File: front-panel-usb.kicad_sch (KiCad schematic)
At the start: 75 parts, among them J3 USB-C_GCT_USB4105-GF-A, J4 USB-C_GCT_USB4105-GF-A, J5 USB-C_GCT_USB4105-GF-A, Q29 BSS84AKW, U11 TPD4E05U06QDQARQ1, U13 FT4232H_VQFN, U15 NCP718BSN330T1G, U3 AP22615A_TSOT26, U5 AP22615A_TSOT26, U6 TPD4E05U06QDQARQ1, U7 TPD4E05U06QDQARQ1, Y1 Resonator_12MHz_ABM8G

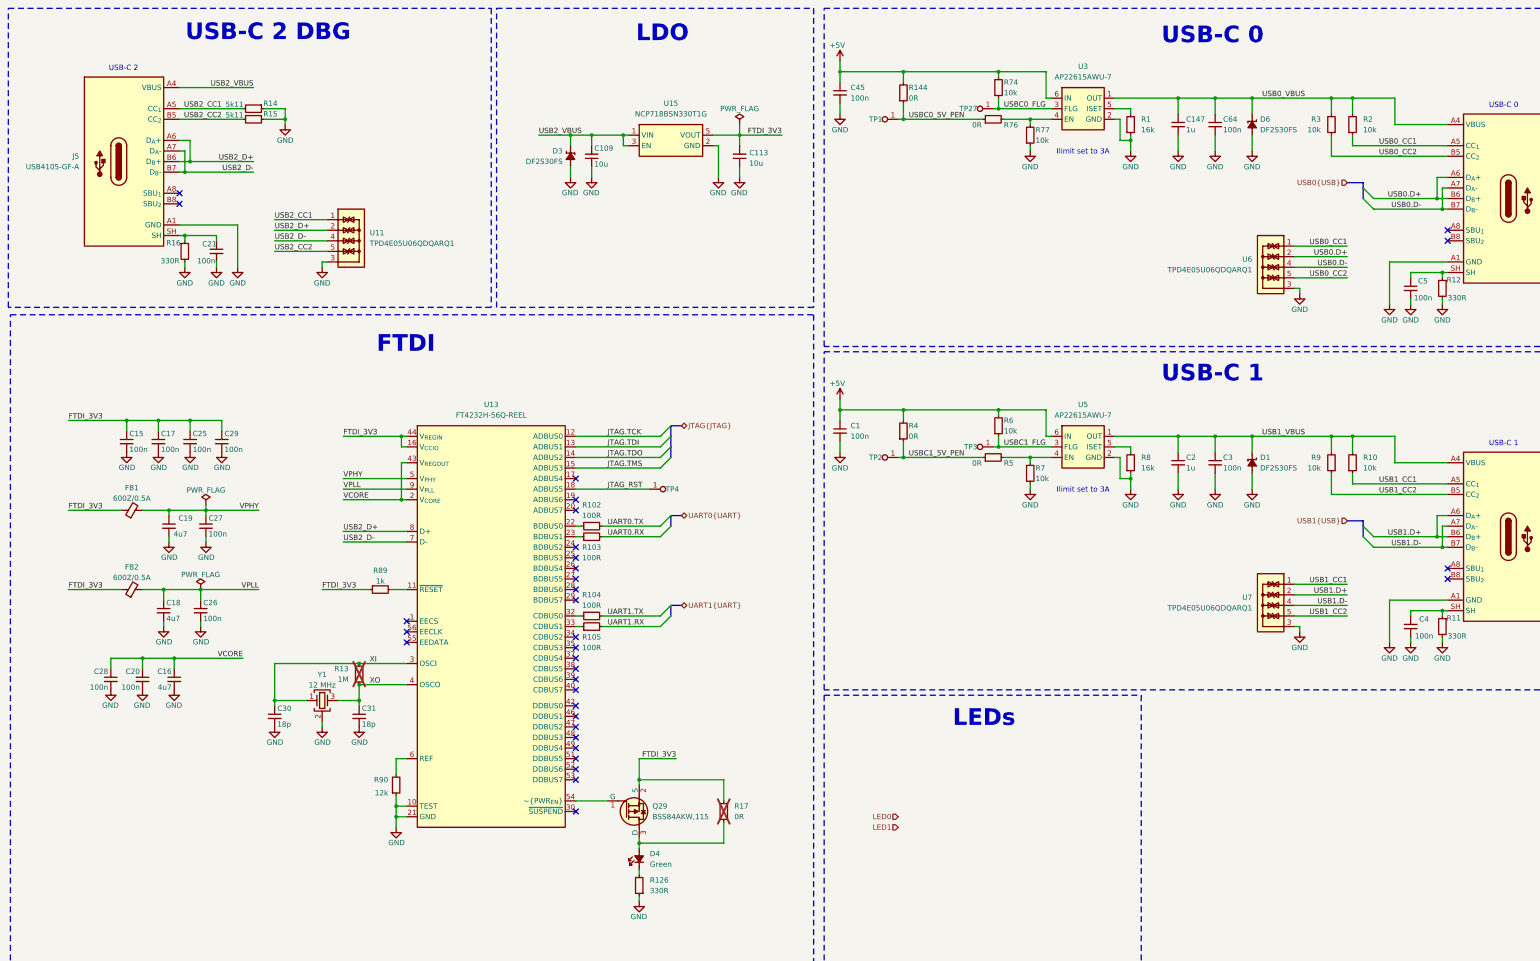
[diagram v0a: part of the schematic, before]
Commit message: [#82176] Fix conflicting annotations
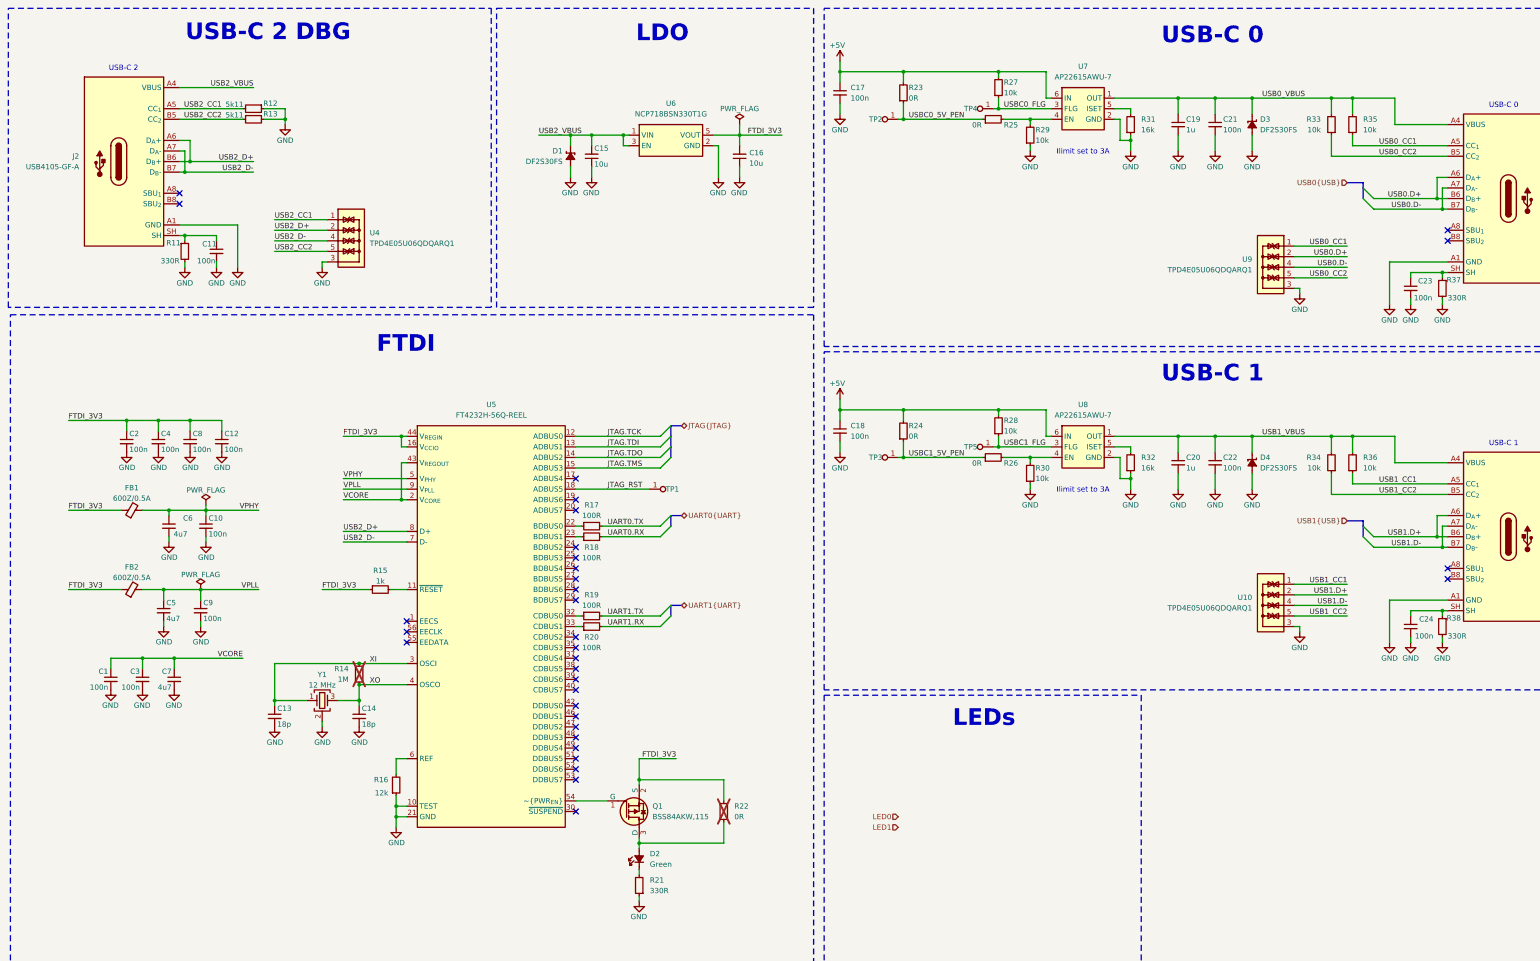
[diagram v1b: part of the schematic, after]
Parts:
- renumbered C28 to C1, C27 to C10, C21 to C11, C29 to C12, C30 to C13, C31 to C14, C109 to C15, C113 to C16, C45 to C17, C1 to C18, C147 to C19, C15 to C2, C2 to C20, C64 to C21, C3 to C22, C5 to C23, C4 to C24, C20 to C3, C17 to C4, C18 to C5, C19 to C6, C16 to C7, C25 to C8, C26 to C9, D3 to D1, D4 to D2, D6 to D3, D1 to D4, J5 to J2, Q29 to Q1, R16 to R11, R14 to R12, R15 to R13, R13 to R14, R89 to R15, R90 to R16, R102 to R17, R103 to R18, R104 to R19, R105 to R20, R126 to R21, R17 to R22, R144 to R23, R4 to R24, R76 to R25, R5 to R26, R74 to R27, R6 to R28, R77 to R29, R7 to R30, R1 to R31, R8 to R32, R3 to R33, R9 to R34, R2 to R35, R10 to R36, R12 to R37, R11 to R38, TP4 to TP1, TP1 to TP2, TP2 to TP3, TP27 to TP4, TP3 to TP5, U7 to U10, U11 to U4, U13 to U5, U15 to U6, U3 to U7, U5 to U8, U6 to U9

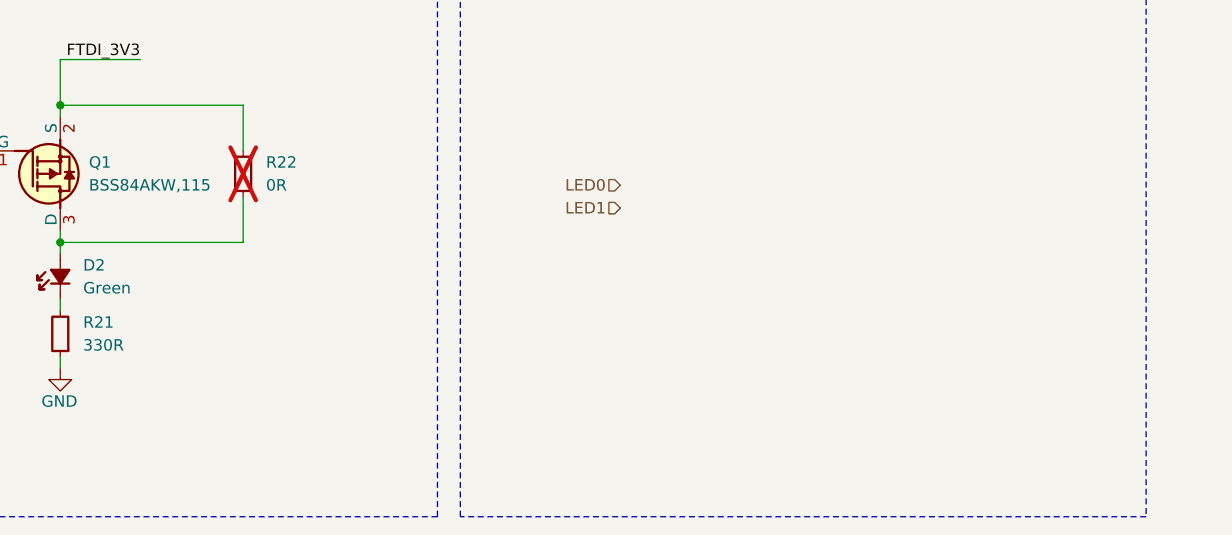
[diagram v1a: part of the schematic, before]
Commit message: Add light pipe and one additional LED
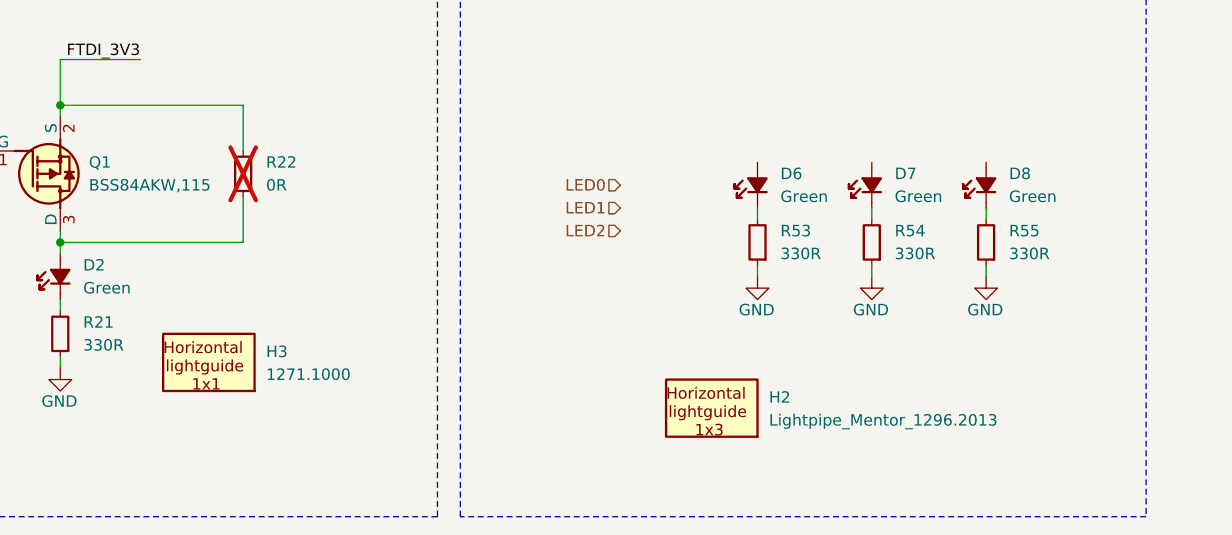
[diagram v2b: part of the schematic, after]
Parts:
- added D6, D7, D8: LED_G_0402_VLMTG1500-GS08, antmicro-footprints:LED_0402_1005Metric_G, symbol antmicroLEDIndicationDiscrete:LED_G_0402_VLMTG1500-GS08
- added H2: Lightpipe_Mentor_1296.2013, antmicro-footprints:Mech_Lightpipe_Mentor_1296.2013, symbol antmicroMechanicalParts:Lightpipe_Mentor_1296.2013
- added H3: Lightpipe_Mentor_1271.1000, antmicro-footprints:Mech_Lightpipe_Mentor_1271.1000, symbol antmicroMechanicalParts:Lightpipe_Mentor_1271.1000
- added R53, R54, R55: R_330R_0402, antmicro-footprints:R_0402_1005Metric, symbol antmicroResistors0402:R_330R_0402
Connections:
- net GND: now also R53.1, R54.1, R55.1
- new net: D7.1 (C), R54.2
- new net: D8.1 (C), R55.2
- new net: D6.1 (C), R53.2

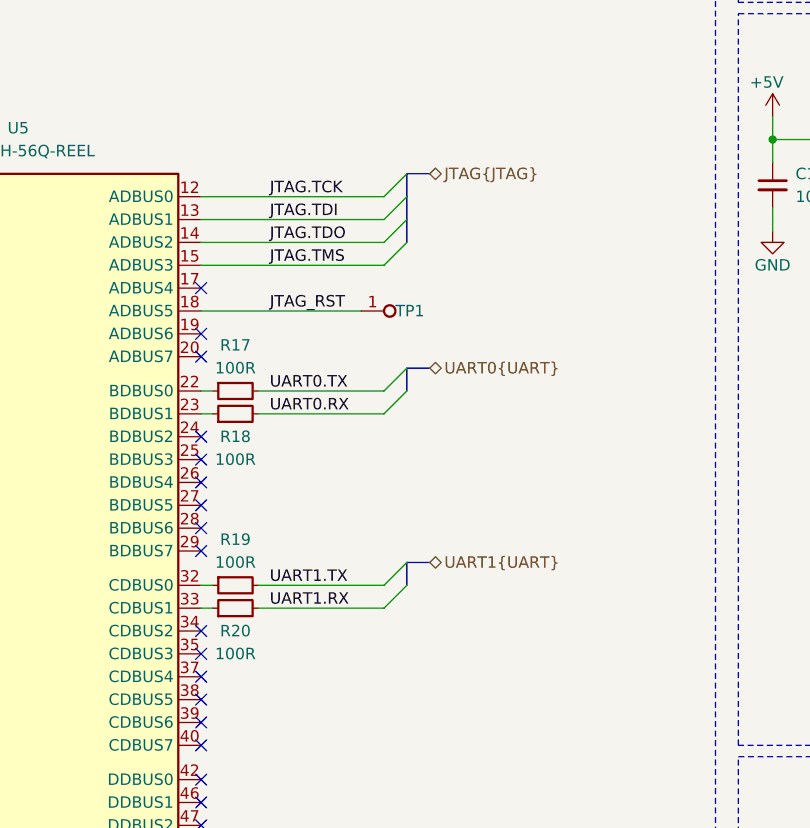
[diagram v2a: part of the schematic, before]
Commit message: Add series resistors to JTAG lines
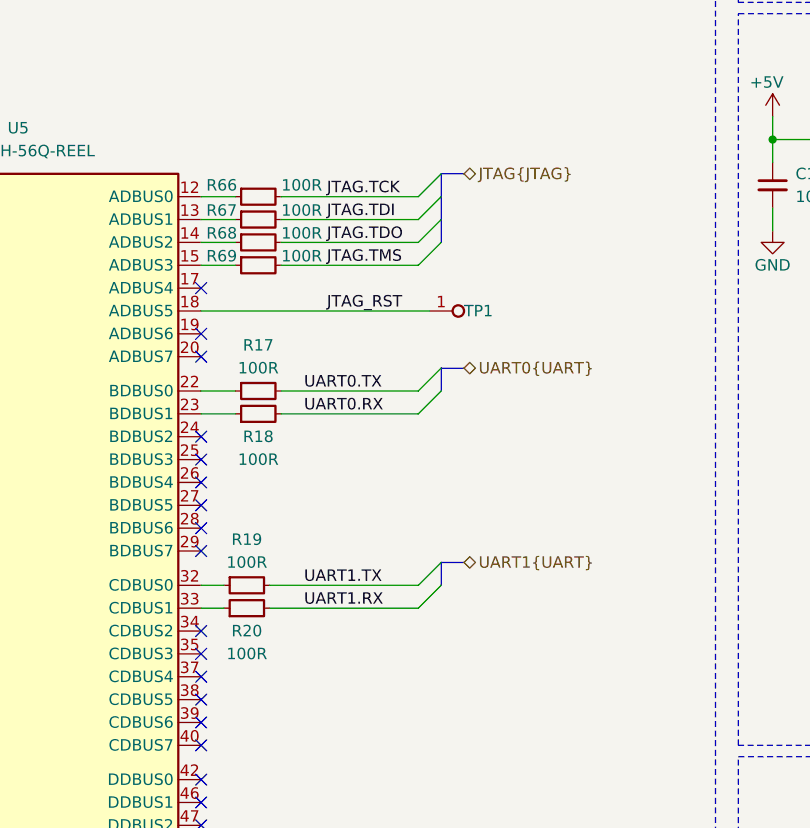
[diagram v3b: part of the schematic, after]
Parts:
- added R66, R67, R68, R69: R_100R_0402, antmicro-footprints:R_0402_1005Metric, symbol antmicroResistors0402:R_100R_0402
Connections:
- net JTAG.TCK: now also R66.2; no longer U5.12 (ADBUS0)
- net JTAG.TDI: now also R67.2; no longer U5.13 (ADBUS1)
- net JTAG.TDO: now also R68.2; no longer U5.14 (ADBUS2)
- net JTAG.TMS: now also R69.2; no longer U5.15 (ADBUS3)
- new net: R66.1, U5.12 (ADBUS0)
- new net: R67.1, U5.13 (ADBUS1)
- new net: R68.1, U5.14 (ADBUS2)
- new net: R69.1, U5.15 (ADBUS3)
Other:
- moved on the sheet: R17, R18, R19, R20, TP1

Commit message: Replace USB-C connectors with vertical version
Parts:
- removed J2, J3, J4: USB-C_GCT_USB4105-GF-A, antmicro-footprints:USB-C_Receptacle_GCT_USB4105-GF-A, symbol antmicroUSBConnectors:USB-C_GCT_USB4105-GF-A
- removed R66, R67, R68, R69: R_100R_0402, antmicro-footprints:R_0402_1005Metric, symbol antmicroResistors0402:R_100R_0402
- added J2, J3, J4: USB-C_Kycon_KUSBX-SL2-CS1N24-B-TR, antmicro-footprints:USB-C_Receptacle_Kycon_KUSBX-SL2-CS1N24-B-TR, symbol antmicroUSBConnectors:USB-C_Kycon_KUSBX-SL2-CS1N24-B-TR
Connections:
- net GND: now also J2.A1 (GND), J2.A12 (GND), J2.B1 (GND), J2.B12 (GND), J3.A1 (GND), J3.A12 (GND), J3.B1 (GND), J3.B12 (GND), J4.A1 (GND), J4.A12 (GND), J4.B1 (GND), J4.B12 (GND)
- net JTAG.TCK: now also U5.12 (ADBUS0)
- net JTAG.TDI: now also U5.13 (ADBUS1)
- net JTAG.TDO: now also U5.14 (ADBUS2)
- net JTAG.TMS: now also U5.15 (ADBUS3)
- net USB0.D+: now also J3.A6 (D_{A}+), J3.B6 (D_{B}+)
- net USB0.D-: now also J3.A7 (D_{A}-), J3.B7 (D_{B}-)
- net USB0_CC1: now also J3.A5 (CC_{1})
- net USB0_CC2: now also J3.B5 (CC_{2})
- net USB0_VBUS: now also J3.A4 (VBUS), J3.A9 (VBUS), J3.B4 (VBUS), J3.B9 (VBUS)
- net USB1.D+: now also J4.A6 (D_{A}+), J4.B6 (D_{B}+)
- net USB1.D-: now also J4.A7 (D_{A}-), J4.B7 (D_{B}-)
- net USB1_CC1: now also J4.A5 (CC_{1})
- net USB1_CC2: now also J4.B5 (CC_{2})
- net USB1_VBUS: now also J4.A4 (VBUS), J4.A9 (VBUS), J4.B4 (VBUS), J4.B9 (VBUS)
- net USB2_CC1: now also J2.A5 (CC_{1})
- net USB2_CC2: now also J2.B5 (CC_{2})
- net USB2_D+: now also J2.A6 (D_{A}+), J2.B6 (D_{B}+)
- net USB2_D-: now also J2.A7 (D_{A}-), J2.B7 (D_{B}-)
- net USB2_VBUS: now also J2.A4 (VBUS), J2.A9 (VBUS), J2.B4 (VBUS), J2.B9 (VBUS)
- net at C23.1, R37.1: now also J3.SH
- net at C11.1, R11.1: now also J2.SH
- net at C24.1, R38.1: now also J4.SH
- no-connect marks 33 -> 57
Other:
- moved on the sheet: C1, C10, C11, C12, C13, C14, C15, C16, C17, C18, C19, C2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
